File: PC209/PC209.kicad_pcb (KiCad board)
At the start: 2 copper layers, 92.5 x 10 mm, 37 parts, among them J1 PC209_BoardEdge_44pin, Q1 BC848W, Q2 BC848W, Q3 BC848W, Q4 BC848W, Q5 BC848W, Q6 BC848W, Q7 BC848W

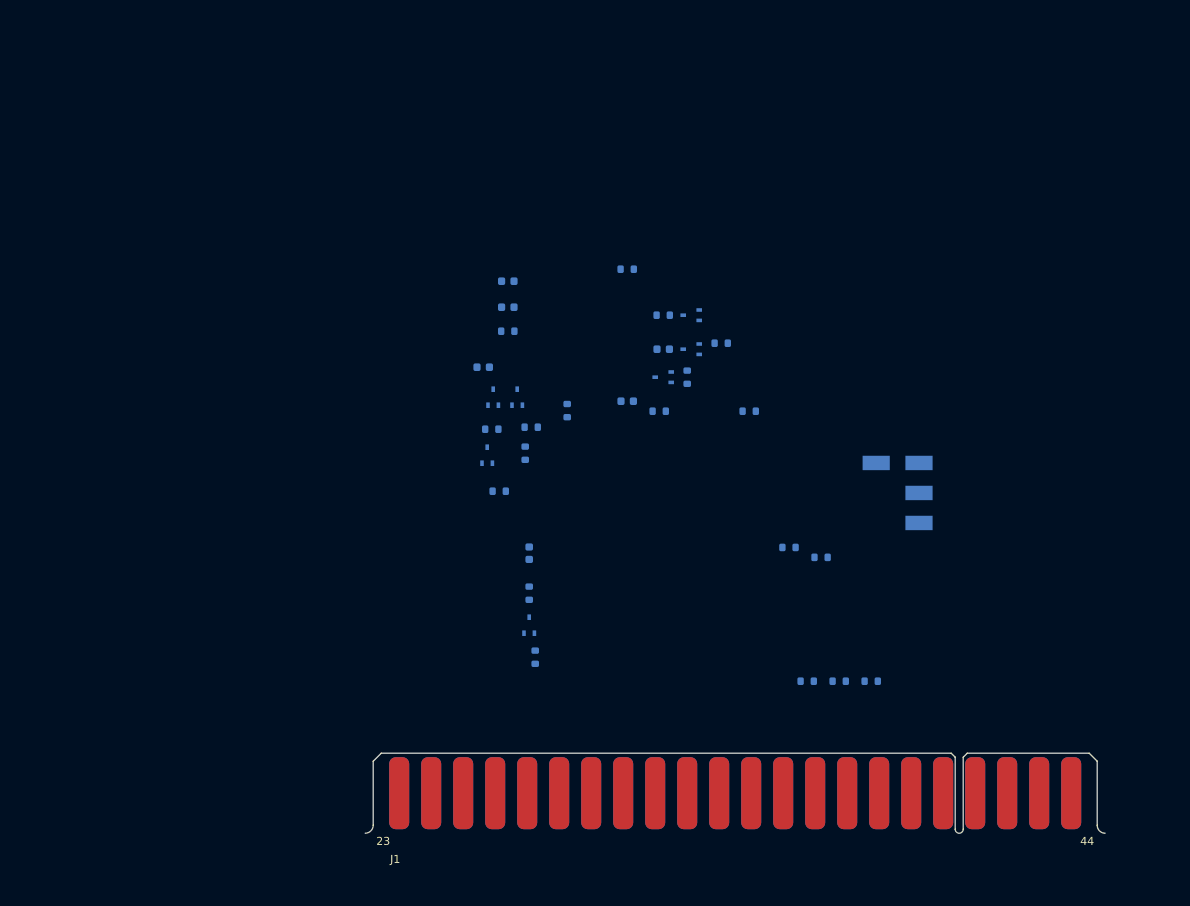
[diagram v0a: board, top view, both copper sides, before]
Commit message: PC209: Initial layout for pulse generator sections
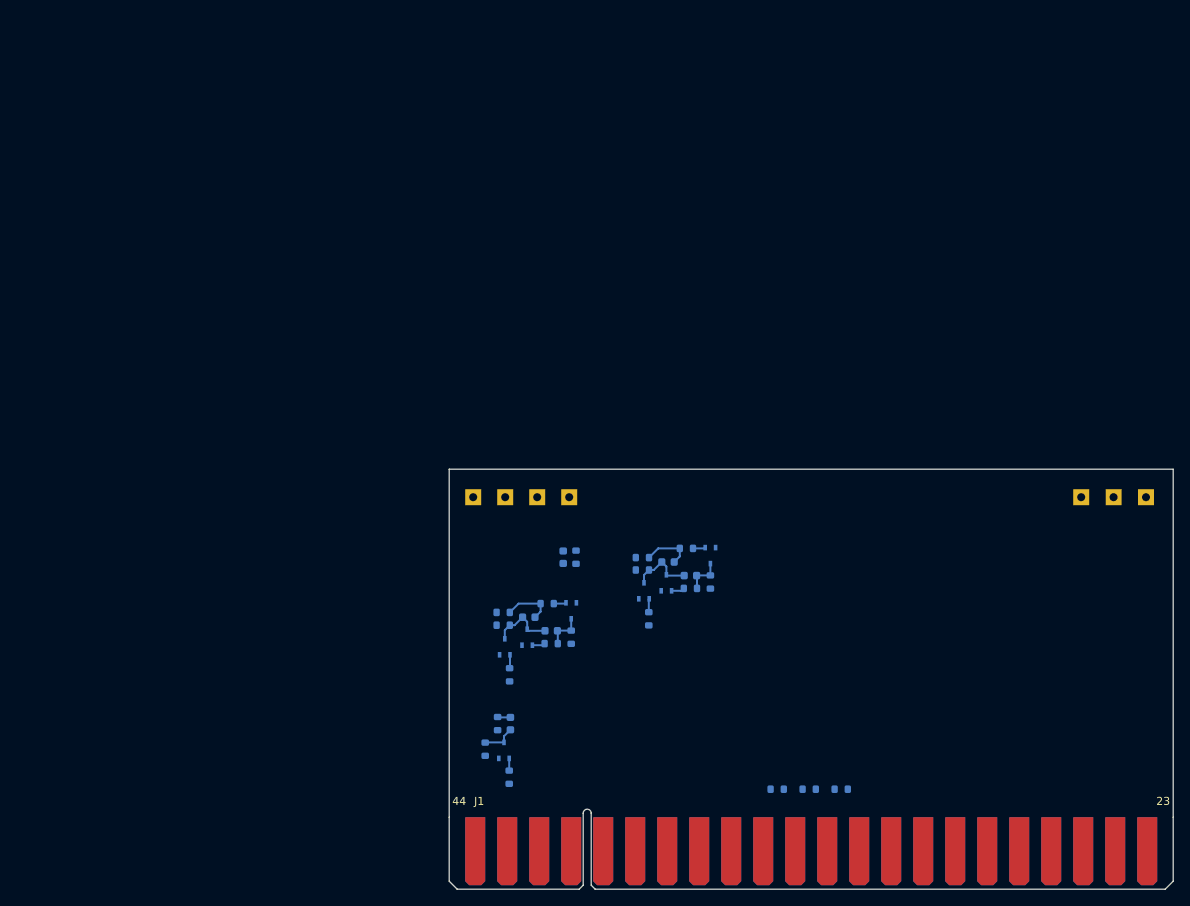
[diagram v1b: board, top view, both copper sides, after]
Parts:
- added TP5: 15 V, TestPoint:TestPoint_THTPad_2.0x2.0mm_Drill1.0mm, B.Cu at (183.0, 100.0)
- added TP6: 3.6 V, TestPoint:TestPoint_THTPad_2.0x2.0mm_Drill1.0mm, B.Cu at (191.1, 100.0)
- added TP7: GND, TestPoint:TestPoint_THTPad_2.0x2.0mm_Drill1.0mm, B.Cu at (187.1, 100.0)
- TP1, TP3: footprint TestPoint:TestPoint_Keystone_5015_Micro-Minature -> TestPoint:TestPoint_THTPad_2.0x2.0mm_Drill1.0mm
- TP2: value 10 us delay -> 10 μs delay; footprint TestPoint:TestPoint_Keystone_5015_Micro-Minature -> TestPoint:TestPoint_THTPad_2.0x2.0mm_Drill1.0mm
- TP4: value 10 us delay -> 100 μs pulse; footprint TestPoint:TestPoint_Keystone_5015_Micro-Minature -> TestPoint:TestPoint_THTPad_2.0x2.0mm_Drill1.0mm
- moved TP1 55.8 mm to (107.0, 100.0)
- moved TP3 51.7 mm to (111.0, 100.0)
- moved TP2 47.9 mm to (115.0, 100.0)
- moved R17 45.6 mm to (110.8, 114.4)
- moved C6 42.1 mm to (114.0, 115.0), turned to 0 degrees
- moved R7 40.0 mm to (128.9, 115.2), turned to 90 degrees
- moved TP4 38.6 mm to (119.0, 100.0)
- moved Q2 35.0 mm to (128.3, 111.7), turned to 90 degrees
- moved C5 34.0 mm to (116.8, 116.7), turned to 180 degrees
- moved R9 34.0 mm to (110.0, 128.3)
- moved C1 32.0 mm to (118.2, 107.5), turned to 90 degrees
- moved R8 32.0 mm to (128.2, 109.1)
- moved Q4 31.2 mm to (111.0, 118.7)
- moved R11 31.1 mm to (111.5, 122.2), turned to 90 degrees
- moved Q5 30.3 mm to (113.8, 117.5)
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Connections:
- TP4 pad 1: unconnected-(TP4-Pad1) -> Print CMD A
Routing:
- net Net-(C1-Pad1): track 0.00 -> 8.02 mm
- net Print CMD A: track 0.00 -> 7.98 mm
- net Net-(C4-Pad2): track 0.00 -> 6.32 mm
- net Net-(C6-Pad2): track 0.00 -> 6.30 mm
- net Net-(C3-Pad1): track 0.00 -> 4.83 mm
- net Net-(C5-Pad1): track 0.00 -> 4.83 mm
- net Net-(C2-Pad1): track 0.00 -> 4.27 mm
- net Net-(Q2-Pad1): track 0.00 -> 1.70 mm
- net Net-(Q4-Pad1): track 0.00 -> 1.70 mm
- net Net-(Q3-Pad1): track 0.00 -> 1.65 mm
- net Net-(C2-Pad2): track 0.00 -> 1.62 mm
- net Net-(Q5-Pad1): track 0.00 -> 1.61 mm
- net Net-(Q6-Pad1): track 0.00 -> 1.57 mm
- net Net-(Q7-Pad1): track 0.00 -> 1.57 mm
- net Net-(Q1-Pad1): track 0.00 -> 1.53 mm
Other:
- board size 92.5 x 10 mm -> 90.5 x 43.5 mm
- board text added: "10 μs delay"
- board text added: "100 μs pulse"

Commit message: PC209: Initial board routing
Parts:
- added C7: 100 pF, Capacitor_SMD:C_0603_1608Metric, B.Cu at (152.7, 114.9)
- added Q10: BC848W, Package_TO_SOT_SMD:SOT-323_SC-70, F.Cu at (127.5, 133.2)
- added Q11: BC848W, Package_TO_SOT_SMD:SOT-323_SC-70, F.Cu at (123.5, 133.2)
- added Q12: BC848W, Package_TO_SOT_SMD:SOT-323_SC-70, F.Cu at (119.5, 133.2)
- added Q13: BC848W, Package_TO_SOT_SMD:SOT-323_SC-70, F.Cu at (139.5, 133.2)
- added Q14: BC848W, Package_TO_SOT_SMD:SOT-323_SC-70, B.Cu at (149.4, 124.8)
- added Q15: BC848W, Package_TO_SOT_SMD:SOT-323_SC-70, B.Cu at (149.4, 114.0)
- added Q16: BC848W, Package_TO_SOT_SMD:SOT-323_SC-70, F.Cu at (107.5, 133.2)
- added Q17: BC848W, Package_TO_SOT_SMD:SOT-323_SC-70, B.Cu at (149.4, 122.1)
- added Q8: BC848W, Package_TO_SOT_SMD:SOT-323_SC-70, F.Cu at (135.5, 133.2)
- added Q9: BC848W, Package_TO_SOT_SMD:SOT-323_SC-70, F.Cu at (131.5, 133.2)
- added R20: 120k, Resistor_SMD:R_0603_1608Metric, F.Cu at (134.8, 136.5)
- added R21: 120k, Resistor_SMD:R_0603_1608Metric, F.Cu at (130.8, 136.5)
- added R22: 120k, Resistor_SMD:R_0603_1608Metric, F.Cu at (126.8, 136.5)
- added R23: 120k, Resistor_SMD:R_0603_1608Metric, F.Cu at (122.8, 136.5)
- added R24: 120k, Resistor_SMD:R_0603_1608Metric, F.Cu at (118.8, 136.5)
- added R25: 180k, Resistor_SMD:R_0603_1608Metric, F.Cu at (135.5, 129.9)
- added R26: 180k, Resistor_SMD:R_0603_1608Metric, F.Cu at (131.5, 129.9)
- added R27: 180k, Resistor_SMD:R_0603_1608Metric, F.Cu at (127.5, 129.9)
- added R28: 180k, Resistor_SMD:R_0603_1608Metric, F.Cu at (123.5, 129.9)
- added R29: 180k, Resistor_SMD:R_0603_1608Metric, F.Cu at (119.5, 129.9)
- added R30: 120k, Resistor_SMD:R_0603_1608Metric, F.Cu at (138.8, 136.5)
- added R31: 180k, Resistor_SMD:R_0603_1608Metric, F.Cu at (139.5, 129.9)
- added R32: 120k, Resistor_SMD:R_0603_1608Metric, B.Cu at (152.7, 124.2)
- added R33: 120k, Resistor_SMD:R_0603_1608Metric, B.Cu at (152.7, 113.4)
- added R34: 1k, Resistor_SMD:R_0603_1608Metric, B.Cu at (106.8, 136.5)
- added R35: 120k, Resistor_SMD:R_0603_1608Metric, F.Cu at (106.8, 136.5)
- added R36: 180k, Resistor_SMD:R_0603_1608Metric, B.Cu at (146.1, 114.0)
- added R37: 180k, Resistor_SMD:R_0603_1608Metric, B.Cu at (146.1, 122.2)
- added R38: 180k, Resistor_SMD:R_0603_1608Metric, F.Cu at (107.5, 129.9)
- added R39: 120k, Resistor_SMD:R_0603_1608Metric, B.Cu at (152.7, 121.5)
- added R40: 0, Resistor_SMD:R_0603_1608Metric, B.Cu at (183.2, 136.5)
- added R41: 0, Resistor_SMD:R_0603_1608Metric, B.Cu at (179.2, 136.5)
- added R42: 0, Resistor_SMD:R_0603_1608Metric, B.Cu at (175.3, 136.5)
- added R43: 0, Resistor_SMD:R_0603_1608Metric, B.Cu at (167.2, 136.5)
- added R44: 0, Resistor_SMD:R_0603_1608Metric, B.Cu at (163.3, 136.5)
- added R45: 0, Resistor_SMD:R_0603_1608Metric, B.Cu at (159.2, 136.5)
- added U1: 4010, Package_SO:SOIC-16_3.9x9.9mm_P1.27mm, B.Cu at (131.4, 131.7)
- added U2: 4010, Package_SO:SOIC-16_3.9x9.9mm_P1.27mm, B.Cu at (115.5, 131.7)
- C2, Q1, R4, R6, R9: moved to F.Cu
- moved R5 11.6 mm to (123.9, 118.4), turned to 0 degrees
- moved C1 10.9 mm to (123.9, 116.8), turned to 0 degrees
- moved TP7 8.72 mm to (191.5, 107.5)
- moved TP6 8.32 mm to (187.5, 107.5)
- moved C4 7.54 mm to (134.2, 115.1)
- moved Q2 7.54 mm to (131.2, 118.7)
- moved R7 7.54 mm to (131.8, 122.2)
- moved C3 7.54 mm to (136.9, 116.8)
- moved Q3 7.54 mm to (133.9, 117.7)
- moved Q6 7.54 mm to (139.4, 114.3)
- moved R10 7.54 mm to (136.9, 118.4)
- moved R13 7.54 mm to (130.9, 114.5)
- moved R14 7.54 mm to (136.4, 113.4)
- moved R16 7.54 mm to (139.4, 117.6)
- moved R8 7.54 mm to (130.9, 116.1)
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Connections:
- C3 pad 2: Print CMD A -> /Pulse Generator/Output
- C4 pad 1: Print CMD A -> /Pulse Generator/Output
- J1 pad 3: Trigger -> Trigger Out
- J1 pad 4: Hold 2 -> Hold 2 Out
- J1 pad 5: Hold 1 -> Hold 1 Out
- J1 pad 7: 1e-2 Range -> Range 1e-2 Out
- J1 pad 8: Range Hold -> Range Hold Out
- J1 pad 9: Zero Check -> Zero Check Out
- Q2 pad 3: Print CMD A -> /Pulse Generator/Output
- Q3 pad 3: Print CMD A -> /Pulse Generator/Output
- R8 pad 1: Print CMD A -> /Pulse Generator/Output
- TP4 pad 1: Print CMD A -> /Pulse Generator/Output
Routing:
- net Net-(Q16-Pad3): track 0.00 -> 61.2 mm, vias 0 -> 2
- net /Pulse Generator/Output: track 0.00 -> 58.3 mm
- net Net-(Q14-Pad3): track 0.00 -> 42.7 mm
- net Net-(Q15-Pad3): track 0.00 -> 42.6 mm, vias 0 -> 2
- net Buffer Storage: track 0.00 -> 38.5 mm, vias 0 -> 1
- net Zero Check: track 0.00 -> 28.2 mm, vias 0 -> 1
- net Range 1 Print: track 0.00 -> 26.5 mm
- net Net-(C1-Pad1): track 8.02 -> 33.5 mm
- net Net-(C2-Pad2): track 1.62 -> 23.4 mm, vias 0 -> 1
- net Zero Check Print: track 0.00 -> 18.3 mm
- net Range 2 Print: track 0.00 -> 18.2 mm
- net Range Signal Print: track 0.00 -> 14.6 mm
- net Net-(Q12-Pad3): track 0.00 -> 14.5 mm, vias 0 -> 1
- net Print CMD B: track 0.00 -> 13.4 mm
- net Net-(C1-Pad2): track 0.00 -> 11.3 mm
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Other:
- board size 90.5 x 43.5 mm -> 90.5 x 36 mm
- board text added: "Print A"
- board text added: "Print B"

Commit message: PC209: Rev 1.0
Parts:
- added REF**: OSHW-Logo_5.7x6mm_SilkScreen, Symbol:OSHW-Logo_5.7x6mm_SilkScreen, B.Cu at (89.9, 43.6)
- added REF**: KiCad-Logo2_5mm_SilkScreen, Symbol:KiCad-Logo2_5mm_SilkScreen, B.Cu at (79.9, 43.6)
- moved C1 88.5 mm to (56.5, 59.7)
- moved Q2 88.5 mm to (57.4, 63.0)
- moved R1 88.5 mm to (53.4, 59.8)
- moved R2 88.5 mm to (58.1, 59.7)
- moved R3 88.5 mm to (65.4, 59.8)
- moved R4 88.5 mm to (69.4, 59.8)
- moved R5 88.5 mm to (73.4, 59.8)
- moved R6 88.5 mm to (77.4, 59.8)
- moved R7 88.5 mm to (81.4, 59.8)
- moved R8 88.5 mm to (85.4, 59.8)
- moved J1 88.5 mm to (49.9, 69.9)
- moved Q1 88.5 mm to (53.4, 63.1)
- moved R15 88.5 mm to (76.7, 66.4)
- moved R16 88.5 mm to (80.7, 66.4)
- moved R17 88.5 mm to (84.7, 66.4)
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- renumbered C2 to C1, C7 to C2, C4 to C3, C6 to C4, C1 to C5, C3 to C6, C5 to C7, Q16 to Q1, Q6 to Q10, Q7 to Q11, Q5 to Q12, Q3 to Q13, Q2 to Q14, Q4 to Q15, Q17 to Q16, Q14 to Q17, Q1 to Q2, Q12 to Q3, Q11 to Q4, Q10 to Q5, Q9 to Q6, Q8 to Q7, Q13 to Q8, Q15 to Q9, R38 to R1, R35 to R10, R4 to R11, R24 to R12, R23 to R13, R22 to R14, R21 to R15, R20 to R16, R30 to R17, R33 to R18, R36 to R19, R9 to R2, R18 to R20, R14 to R21, R13 to R22, R17 to R23, R8 to R24, R12 to R25, R16 to R26, R19 to R27, R5 to R28, R15 to R29, R29 to R3, R10 to R30, R39 to R31, R37 to R32, R7 to R33, R11 to R34, R32 to R35, R40 to R36, R41 to R37, R42 to R38, R43 to R39, R28 to R4, R44 to R40, R45 to R41, R1 to R42, R2 to R43, R3 to R44, R34 to R45, R27 to R5, R26 to R6, R25 to R7, R31 to R8, R6 to R9, TP7 to TP1, TP6 to TP2, TP5 to TP3, TP2 to TP5, TP3 to TP6, TP1 to TP7
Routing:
- net +15V: track 0.00 -> 179.1 mm, vias 0 -> 7
- net +3.6V: track 0.00 -> 131.5 mm, vias 0 -> 5
- net /Pulse Generator/Output: track 58.3 -> 100.0 mm, vias 0 -> 1
- net Net-(Q15-Pad3): track 42.6 -> 83.0 mm
- net Net-(Q14-Pad3): track 42.7 -> 82.6 mm
- net Net-(Q16-Pad3): track 61.2 -> 98.9 mm, vias 2 -> 1
- net Net-(C2-Pad2): track 23.4 -> 57.4 mm
- net Net-(C1-Pad1): track 33.5 -> 57.9 mm, vias 0 -> 1
- net GND: track 0.00 -> 16.3 mm, vias 0 -> 107
- net Buffer Storage: track 38.5 -> 36.6 mm, vias 1 -> 0
- net Zero Check Print: track 18.3 -> 17.0 mm
- net Print CMD B: track 13.4 -> 12.7 mm
- net Net-(C1-Pad2): track 11.3 -> 10.7 mm
- added copper zone on B.Cu, net GND
- added copper zone on F.Cu, net GND
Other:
- board size 90.5 x 36 mm -> 90.5 x 30 mm
- board text added: "+15V"
- board text added: "+3.6V"
- board text added: "Delay"
- board text added: "GND"
- board text added: "Inv"
- board text added: "Keithley 615 PC209 Replacement V1.0 Peter Farley, 2023"
- board text added: "Pulse"
- board text added: "Store"

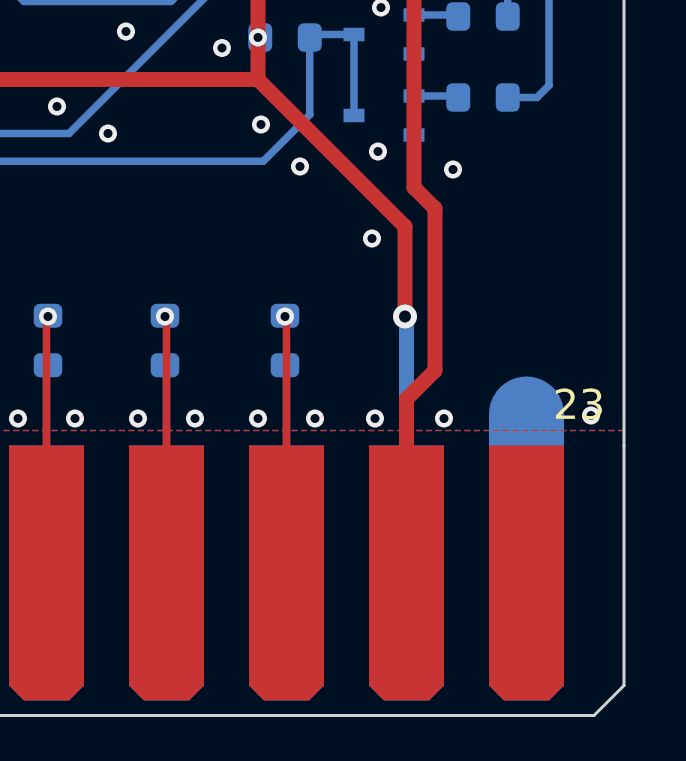
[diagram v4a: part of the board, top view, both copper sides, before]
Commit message: PC209: Fix position of -15 V and +3.6 V on card edge
Update component values
Make library path relative
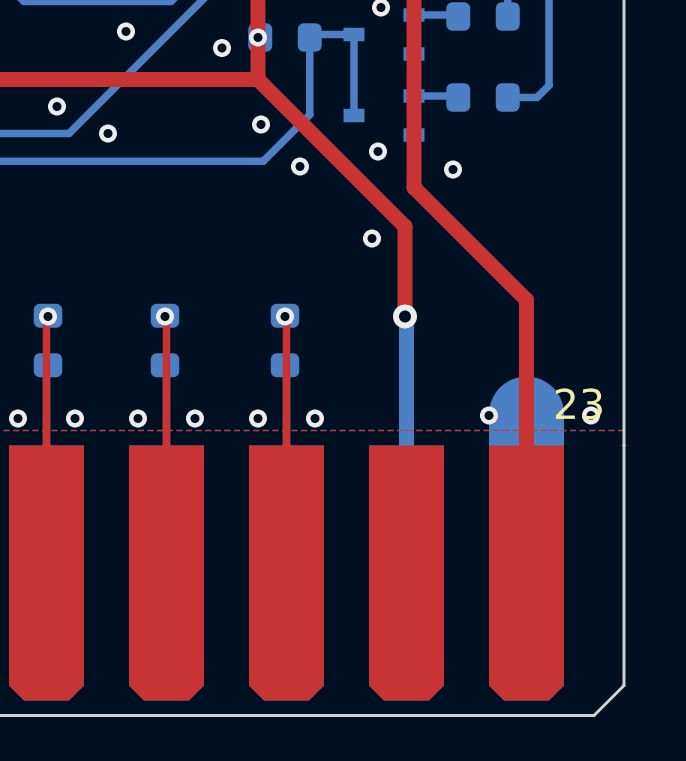
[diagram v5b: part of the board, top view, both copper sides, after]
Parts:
- R11, R20, R21, R29, R30, R33, R34: value 450 -> 453
- R23: value 303k -> 3.3k
- R24, R25, R26, R27: value 640 -> 634
- R9: value 450 -> 634
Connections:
- J1 pad 23: -15V -> +3.6V
- J1 pad 24: +3.6V -> -15V
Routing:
- net +3.6V: track 131.5 -> 132.3 mm
- net GND: vias 107 -> 106
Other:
- board text added: "Keithley 615 PC209 Replacement V1.1 Peter Farley, 2023"
- board text removed: "Keithley 615 PC209 Replacement V1.0 Peter Farley, 2023"
